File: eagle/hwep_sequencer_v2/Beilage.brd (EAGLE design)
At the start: 251.5 x 94 mm, 145 parts, among them X1 ESP32-DEVKIT-C

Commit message: i2s testing & KUB
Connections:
- new net N$1: X2.1
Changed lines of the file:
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@@
 <layer number="25" name="tNames" color="7" fill="1" visible="yes" active="yes"/>
 <layer number="26" name="bNames" color="7" fill="1" visible="yes" active="yes"/>
-<layer number="27" name="tValues" color="7" fill="1" visible="yes" active="yes"/>
-<layer number="28" name="bValues" color="7" fill="1" visible="yes" active="yes"/>
+<layer number="27" name="tValues" color="7" fill="1" visible="no" active="yes"/>
+<layer number="28" name="bValues" color="7" fill="1" visible="no" active="yes"/>
 <layer number="29" name="tStop" color="7" fill="3" visible="no" active="yes"/>
 <layer number="30" name="bStop" color="7" fill="6" visible="no" active="yes"/>
@@
 <via x="171.45" y="71.12" extent="1-16" drill="0.7" diameter="1.4"/>
 </signal>
+<signal name="N$1">
+<contactref element="X2" pad="1"/>
+</signal>
 </signals>

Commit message: removed key register visualisation
bloat feature
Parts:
- removed C24, C25: 1u, rcl_GruS:C0805
- removed C26, C27: 100n, rcl_GruS:C0805
- removed D10: STP16CP05TTR, ic_GruS:TSSOP24
- removed D11: 74AHC1G125DBV, 74xx_GruS:SOT23-5
- removed H18, H19, H20, H21, H22, H23, H24, H25, H26, H27, H28, H29, H30, H31, H32, H33: rt, led_GruS:CHIPLED_1206
- removed R27: 10k, rcl_GruS:R0805
- removed R28: 2k7, rcl_GruS:R0805
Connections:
- net CLRR renamed RKR
- removed net N$10: D10.5, H18.C
- removed net N$11: D10.6, H19.C
- removed net N$12: D10.7, H20.C
- removed net N$13: D10.8, H21.C
- removed net N$20: D10.9, H22.C
- removed net N$21: D10.10, H23.C
- removed net N$22: D10.11, H24.C
- removed net N$23: D10.12, H25.C
- removed net N$24: D10.23, R28.2
- removed net N$25: D10.13, H26.C
- removed net N$26: D10.14, H27.C
- removed net N$27: D10.15, H28.C
- removed net N$28: D10.16, H29.C
- removed net N$29: D10.17, H30.C
- removed net N$30: D10.18, H31.C
- removed net N$31: D10.19, H32.C
- removed net N$32: D10.20, H33.C
- removed net N$66: D10.4, D11.4, R27.2
- net +3V3: no longer C24.1, C25.1, C26.1, C27.1, D10.24, D11.2, D11.5, H18.A, H19.A, H20.A, H21.A, H22.A, H23.A, H24.A, H25.A, H26.A, H27.A, H28.A, H29.A, H30.A, H31.A, H32.A, H33.A
- net GND: no longer C24.2, C25.2, C26.2, C27.2, D10.1, D10.21, D11.3, R27.1, R28.1
- net MOSI: no longer D10.2
- net SCK: no longer D10.3
- net STP_LE_K: no longer D11.1
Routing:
- net N$10: track 44.8 -> 0.00 mm, vias 1 -> 0
- net N$11: track 42.0 -> 0.00 mm, vias 1 -> 0
- net SCK: track 171.0 -> 130.8 mm
- net N$12: track 39.2 -> 0.00 mm, vias 1 -> 0
- net N$13: track 36.4 -> 0.00 mm, vias 1 -> 0
- net N$29: track 34.8 -> 0.00 mm, vias 1 -> 0
- net N$30: track 34.0 -> 0.00 mm, vias 1 -> 0
- net N$28: track 33.7 -> 0.00 mm, vias 1 -> 0
- net N$20: track 33.6 -> 0.00 mm, vias 1 -> 0
- net N$27: track 33.5 -> 0.00 mm, vias 1 -> 0
- net N$26: track 33.2 -> 0.00 mm, vias 1 -> 0
- net N$31: track 33.2 -> 0.00 mm, vias 1 -> 0
- net N$32: track 31.7 -> 0.00 mm, vias 1 -> 0
- net MOSI: track 124.2 -> 92.7 mm, vias 3 -> 2
- net N$21: track 30.8 -> 0.00 mm, vias 1 -> 0
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
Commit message: upd doku
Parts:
- added FABRICATION: (no value), fabrication:FABRIACTION
- added MEASURE: (no value), fabrication:MEASURE
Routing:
- net +3V3: vias 7 -> 6

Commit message: removed unnecessary features
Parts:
- removed C2: 1u, rcl_GruS:C0805
- removed D4: 74AHC138N, 74xx_GruS:DIP16
- moved R7 55.0 mm to (232.4, 29.2)
- moved H2 54.8 mm to (234.9, 29.2)
- moved R1 35.4 mm to (226.1, 33.0), turned to 270 degrees
- moved C3 24.4 mm to (232.4, 80.0)
- moved R20 19.0 mm to (212.1, 72.4)
- moved D3 18.1 mm to (223.5, 73.7)
- moved R17 16.5 mm to (212.1, 67.3)
- moved R22 16.5 mm to (212.1, 77.5), flipped to the top, turned to 0 degrees
- moved H15 15.2 mm to (204.5, 74.9)
- moved H16 15.2 mm to (194.3, 74.9)
- moved H17 15.2 mm to (184.2, 74.9)
- moved V1 15.2 mm to (208.3, 66.0)
- moved V2 15.2 mm to (198.1, 66.0)
- moved V3 15.2 mm to (186.7, 66.0)
- moved R24 14.0 mm to (208.3, 63.5)
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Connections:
- removed net !CS!_A: D4.1, X1.29
- removed net !CS!_B: D4.2, X1.33
- removed net !CS!_C: D4.3, X1.36
- removed net 088S052_!CS!: D4.12, D5.1, R15.1
- removed net N$1: X2.1
- removed net STP_LE_K: D4.13
- removed net STP_LE_S: D13.1, D4.14
- new net ADC088S052_!CS: D5.1, R15.1, X1.33
- new net STP_!CS: D13.1, X1.36
- net +3V3: no longer C2.1, D4.16, D4.6
- net 23S08_!CS: now also X1.29; no longer D4.15
- net GND: now also X2.1; no longer C2.2, D4.4, D4.5, D4.8
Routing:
- net +3V3: track 849.4 -> 764.0 mm, vias 6 -> 5
- net 088S052_!CS!: track 82.0 -> 0.00 mm
- net ADC088S052_!CS: track 0.00 -> 72.8 mm, vias 0 -> 1
- net !CS!_A: track 71.4 -> 0.00 mm, vias 2 -> 0
- net STP_!CS: track 0.00 -> 64.7 mm, vias 0 -> 2
- net !CS!_B: track 60.9 -> 0.00 mm
- net !CS!_C: track 48.7 -> 0.00 mm, vias 1 -> 0
- net 23S08_!CS: track 82.6 -> 130.5 mm
- net STP_LE_S: track 44.6 -> 0.00 mm, vias 1 -> 0
- net 7SEG_C: track 24.9 -> 6.65 mm, vias 1 -> 0
- net 7SEG_D: track 24.1 -> 6.86 mm
- net 7SEG_G: track 22.1 -> 7.94 mm
- net 7SEG_B: track 18.3 -> 5.81 mm, vias 1 -> 0
- net 7SEG_A: track 17.8 -> 6.33 mm, vias 1 -> 0
- net 7SEG_DP: track 17.2 -> 5.81 mm, vias 1 -> 0
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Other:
- board size 251.5 x 94 mm -> 251.5 x 99.1 mm

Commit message: spi test
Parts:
- moved C3 7.73 mm to (224.8, 81.3), turned to 0 degrees
- moved H1 2.54 mm to (167.6, 83.8)
- moved R6 2.54 mm to (170.2, 83.8)
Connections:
- net ADC088S052_!CS: now also X1.23; no longer X1.33
- net INT_23S08: now also X1.36
- net STP_!CS: now also X1.33; no longer X1.36
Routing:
- net INT_23S08: track 2.14 -> 63.9 mm
- net +3V3: track 764.0 -> 822.0 mm
- net STP_!CS: track 64.7 -> 69.4 mm
- net SCK: track 140.0 -> 143.2 mm
- net 23S08_!CS: track 130.5 -> 127.7 mm
- net EVENT: track 28.1 -> 25.6 mm
- net ADC088S052_!CS: track 72.8 -> 70.9 mm
- net GND: track 31.1 -> 31.4 mm, vias 12 -> 15

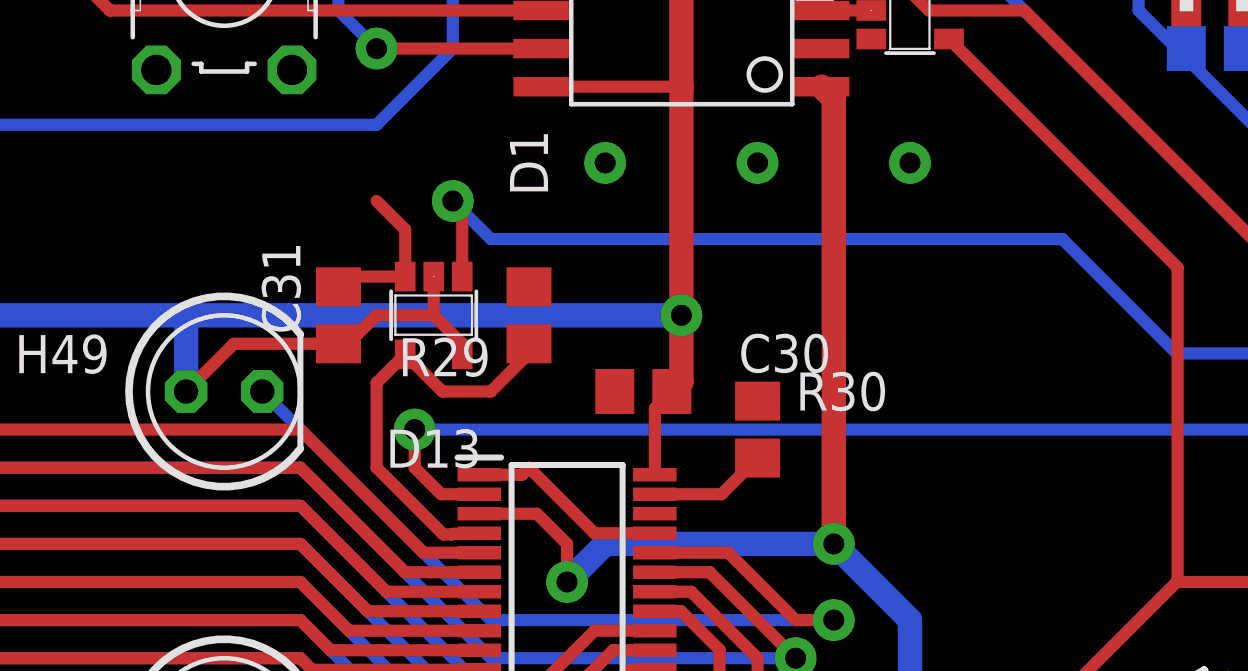
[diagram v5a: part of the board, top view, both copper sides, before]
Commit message: mcp23s08 implemented
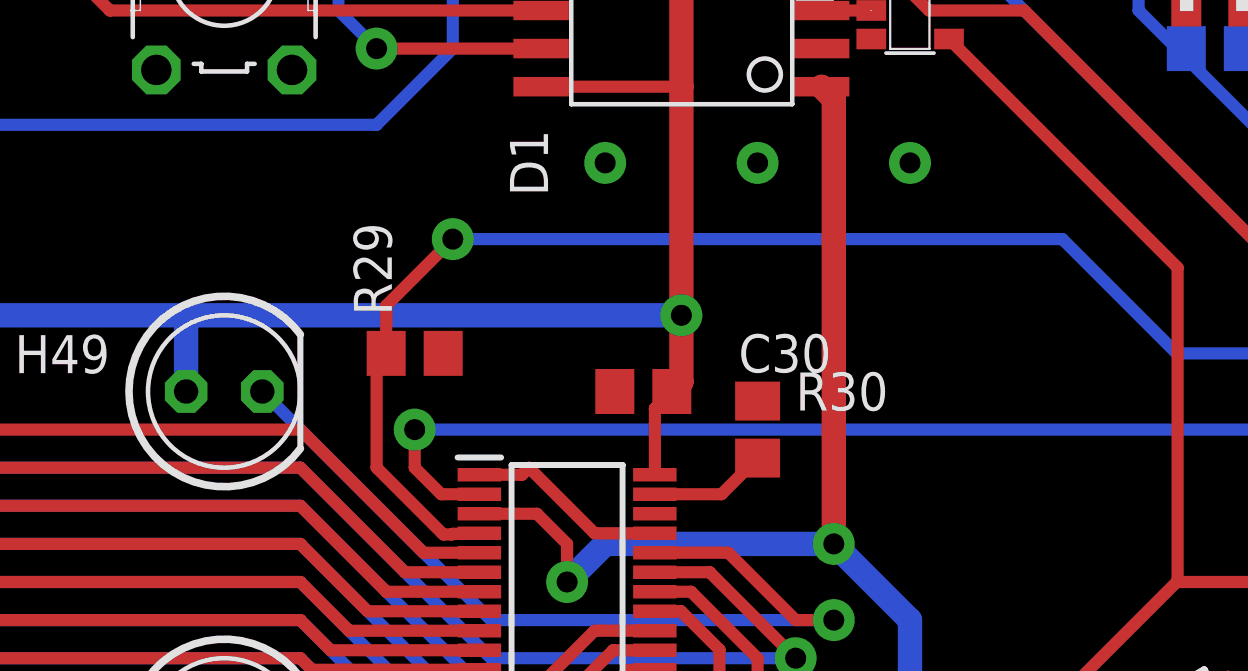
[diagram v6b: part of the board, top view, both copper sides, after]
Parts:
- removed C31: 100n, rcl_GruS:C0805
- removed D13: 74AHC1G125DBV, 74xx_GruS:SOT23-5
- moved R29 4.02 mm to (160.0, 53.3), turned to 180 degrees
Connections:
- removed net N$61: D12.4, D13.4, R29.2
- removed net STP_!CS: D13.1, X1.33
- new net STP_CS: D12.4, R29.2, X1.33
- net +3V3: no longer C31.1, D13.2, D13.5
- net GND: no longer C31.2, D13.3
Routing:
- net STP_CS: track 0.00 -> 79.3 mm, vias 0 -> 2
- net STP_!CS: track 69.4 -> 0.00 mm, vias 2 -> 0
- net N$61: track 14.0 -> 0.00 mm
- net +3V3: track 822.0 -> 809.7 mm
- net GND: track 31.4 -> 26.1 mm
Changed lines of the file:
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@@
 <attribute name="VALUE" x="168.275" y="20.32" size="1.27" layer="27" font="vector" ratio="12" rot="R180"/>
 </element>
-<element name="R29" library="rcl_GruS" library_urn="urn:adsk.eagle:library:13572313" package="R0805" package3d_urn="urn:adsk.eagle:package:18365371/1" value="10k" x="163.83" y="54.61" smashed="yes" rot="R270">
-<attribute name="NAME" x="162.56" y="53.848" size="1.27" layer="25" font="vector" ratio="12" rot="R180"/>
-<attribute name="VALUE" x="162.687" y="55.88" size="1.27" layer="27" font="vector" ratio="12" rot="R180"/>
-</element>
-<element name="C31" library="rcl_GruS" library_urn="urn:adsk.eagle:library:13572313" package="C0805" package3d_urn="urn:adsk.eagle:package:23617/2" value="100n" x="157.48" y="54.61" smashed="yes" rot="R90">
-<attribute name="CATEGORY" value="2" x="157.48" y="54.61" size="1.778" layer="27" rot="R90" display="off"/>
-<attribute name="NAME" x="156.21" y="53.975" size="1.27" layer="25" font="vector" ratio="12" rot="R90"/>
-<attribute name="VALUE" x="160.02" y="51.435" size="1.27" layer="27" font="vector" ratio="12" rot="R90"/>
+<element name="R29" library="rcl_GruS" library_urn="urn:adsk.eagle:library:13572313" package="R0805" package3d_urn="urn:adsk.eagle:package:18365371/1" value="10k" x="160.02" y="53.34" smashed="yes" rot="R180">
+<attribute name="NAME" x="159.258" y="54.61" size="1.27" layer="25" font="vector" ratio="12" rot="R90"/>
+<attribute name="VALUE" x="161.29" y="54.483" size="1.27" layer="27" font="vector" ratio="12" rot="R90"/>
 </element>
 <element name="H3" library="led_GruS" library_urn="urn:adsk.eagle:library:13581853" package="WS2812B" package3d_urn="urn:adsk.eagle:package:33577031/2" value="WS2812B" x="212.09" y="24.13" smashed="yes" rot="R90">
@@
 <attribute name="NAME" x="140.462" y="84.201" size="1.27" layer="25" ratio="10"/>
 <attribute name="VALUE" x="142.875" y="81.661" size="1.27" layer="27" ratio="10" rot="R270"/>
-</element>
-<element name="D13" library="74xx_GruS" library_urn="urn:adsk.eagle:library:13569359" package="SOT23-5" package3d_urn="urn:adsk.eagle:package:33442082/1" value="74AHC1G125DBV" x="160.655" y="54.61" smashed="yes" rot="R180">
-<attribute name="CATEGORY" value="13" x="174.625" y="46.99" size="1.778" layer="27" rot="R180" display="off"/>
-<attribute name="NAME" x="160.655" y="50.8" size="1.27" layer="25" font="vector" rot="R180" align="bottom-center"/>
-<attribute name="VALUE" x="160.655" y="52.07" size="1.27" layer="27" font="vector" rot="R180" align="bottom-center"/>
 </element>
 <element name="X4" library="con_GruS" library_urn="urn:adsk.eagle:library:13569504" package="MYLIB_SJ" package3d_urn="urn:adsk.eagle:package:33704775/1" value="" x="243.84" y="8.89" smashed="yes" rot="R180">
@@
 <via x="238.76" y="15.24" extent="1-16" drill="0.7" diameter="1.4"/>
 <contactref element="D2" pad="3"/>
-<contactref element="C31" pad="2"/>
 <contactref element="H3" pad="3"/>
 <contactref element="H6" pad="3"/>
@@
 <via x="172.72" y="77.47" extent="1-16" drill="0.7" diameter="1.4"/>
 <contactref element="S15" pad="C1"/>
-<contactref element="D13" pad="3"/>
 <contactref element="X3" pad="1"/>
 <wire x1="247.65" y1="24.13" x2="242.57" y2="24.13" width="0.8128" layer="16"/>
@@
 <wire x1="239.268" y1="24.13" x2="242.57" y2="24.13" width="0.8128" layer="16"/>
 <contactref element="R29" pad="1"/>
-<wire x1="157.48" y1="55.56" x2="157.82" y2="55.9" width="0.4064" layer="1"/>
-<wire x1="157.82" y1="55.9" x2="159.705" y2="55.9" width="0.4064" layer="1"/>
 <contactref element="X2" pad="1"/>
 <via x="176.53" y="59.69" extent="1-16" drill="0.7" diameter="1.4"/>
@@
 <via x="217.17" y="57.15" extent="1-16" drill="0.7" diameter="1.4"/>
 <via x="213.36" y="34.29" extent="1-16" drill="0.7" diameter="1.4"/>
-<wire x1="159.705" y1="55.9" x2="159.705" y2="57.465" width="0.4064" layer="1"/>
-<wire x1="159.705" y1="57.465" x2="158.75" y2="58.42" width="0.4064" layer="1"/>
 </signal>
 <signal name="RKR">
@@
 <wire x1="158.75" y1="60.96" x2="137.4394" y2="60.96" width="0.4064" layer="16"/>
 <wire x1="137.4394" y1="60.96" x2="135.6106" y2="62.7888" width="0.4064" layer="16"/>
-</signal>
-<signal name="STP_!CS">
-<contactref element="D13" pad="1"/>
-<contactref element="X1" pad="33"/>
-<wire x1="222.25" y1="44.45" x2="209.55" y2="44.45" width="0.4064" layer="1"/>
-<wire x1="209.55" y1="44.45" x2="200.66" y2="53.34" width="0.4064" layer="1"/>
-<via x="200.66" y="53.34" extent="1-16" drill="0.7" diameter="1.4"/>
-<wire x1="200.66" y1="53.34" x2="185.42" y2="53.34" width="0.4064" layer="16"/>
-<wire x1="185.42" y1="53.34" x2="181.61" y2="57.15" width="0.4064" layer="16"/>
-<wire x1="161.605" y1="55.9" x2="161.605" y2="58.105" width="0.4064" layer="1"/>
-<wire x1="161.605" y1="58.105" x2="161.29" y2="58.42" width="0.4064" layer="1"/>
-<via x="161.29" y="58.42" extent="1-16" drill="0.7" diameter="1.4"/>
-<wire x1="161.29" y1="58.42" x2="162.56" y2="57.15" width="0.4064" layer="16"/>
-<wire x1="162.56" y1="57.15" x2="181.61" y2="57.15" width="0.4064" layer="16"/>
 </signal>
 <signal name="7SEG_CH">
@@
 <contactref element="R1" pad="2"/>
 <contactref element="R15" pad="2"/>
-<contactref element="C31" pad="1"/>
 <wire x1="43.495" y1="52.07" x2="50.8" y2="52.07" width="0.8128" layer="1"/>
 <wire x1="50.8" y1="40.64" x2="43.495" y2="40.64" width="0.8128" layer="1"/>
@@
 <wire x1="106.68" y1="62.23" x2="109.22" y2="62.23" width="0.8128" layer="16"/>
 <wire x1="109.22" y1="62.23" x2="111.76" y2="62.23" width="0.8128" layer="16"/>
-<contactref element="D13" pad="2"/>
-<contactref element="D13" pad="5"/>
-<wire x1="161.605" y1="53.31" x2="161.605" y2="53.66" width="0.4064" layer="1"/>
-<wire x1="161.605" y1="53.66" x2="160.655" y2="54.61" width="0.4064" layer="1"/>
-<wire x1="160.655" y1="55.9" x2="160.655" y2="54.61" width="0.4064" layer="1"/>
 <wire x1="10.16" y1="40.64" x2="12.7" y2="38.1" width="0.8128" layer="16"/>
 <wire x1="12.7" y1="38.1" x2="30.48" y2="38.1" width="0.8128" layer="16"/>
@@
 <wire x1="121.92" y1="62.23" x2="121.92" y2="54.61" width="0.8128" layer="16"/>
 <wire x1="182.88" y1="8.89" x2="223.52" y2="8.89" width="0.8128" layer="16"/>
-<wire x1="152.4" y1="52.07" x2="153.99" y2="53.66" width="0.4064" layer="1"/>
-<wire x1="153.99" y1="53.66" x2="157.48" y2="53.66" width="0.4064" layer="1"/>
-<wire x1="157.48" y1="53.66" x2="157.8" y2="53.66" width="0.4064" layer="1"/>
-<wire x1="157.8" y1="53.66" x2="158.75" y2="54.61" width="0.4064" layer="1"/>
-<wire x1="158.75" y1="54.61" x2="160.655" y2="54.61" width="0.4064" layer="1"/>
 <wire x1="10.16" y1="40.64" x2="10.16" y2="52.07" width="0.8128" layer="16"/>
 <wire x1="242.89" y1="26.67" x2="242.89" y2="29.21" width="0.8128" layer="1"/>
@@
 <contactref element="D1" pad="3"/>
 <wire x1="175.24" y1="64.77" x2="173.585" y2="64.77" width="0.4064" layer="1"/>
-</signal>
-<signal name="N$61">
-<contactref element="D12" pad="4"/>
-<wire x1="162.175" y1="47.345" x2="162.1564" y2="47.3264" width="0.4064" layer="1"/>
-<wire x1="162.1564" y1="47.3264" x2="161.2816625" y2="47.3264" width="0.4064" layer="1"/>
-<wire x1="161.2816625" y1="47.3264" x2="161.2598625" y2="47.3046" width="0.4064" layer="1"/>
-<wire x1="160.9754" y1="47.3046" x2="158.75" y2="49.53" width="0.4064" layer="1"/>
-<wire x1="161.2598625" y1="47.3046" x2="160.9754" y2="47.3046" width="0.4064" layer="1"/>
-<contactref element="D13" pad="4"/>
-<contactref element="R29" pad="2"/>
-<wire x1="159.705" y1="53.31" x2="160.945" y2="52.07" width="0.4064" layer="1"/>
-<wire x1="162.56" y1="52.07" x2="163.83" y2="53.34" width="0.4064" layer="1"/>
-<wire x1="163.83" y1="53.34" x2="163.83" y2="53.66" width="0.4064" layer="1"/>
-<wire x1="160.945" y1="52.07" x2="162.56" y2="52.07" width="0.4064" layer="1"/>
-<wire x1="158.75" y1="49.53" x2="158.75" y2="52.355" width="0.4064" layer="1"/>
-<wire x1="158.75" y1="52.355" x2="159.705" y2="53.31" width="0.4064" layer="1"/>
 </signal>
 <signal name="N$68">
@@
 <wire x1="224.79" y1="54.61" x2="223.52" y2="55.88" width="0.4064" layer="16"/>
 </signal>
+<signal name="STP_CS">
+<contactref element="D12" pad="4"/>
+<contactref element="R29" pad="2"/>
+<wire x1="162.175" y1="47.345" x2="162.1564" y2="47.3264" width="0.4064" layer="1"/>
+<wire x1="162.1564" y1="47.3264" x2="161.2816625" y2="47.3264" width="0.4064" layer="1"/>
+<wire x1="161.2816625" y1="47.3264" x2="161.2598625" y2="47.3046" width="0.4064" layer="1"/>
+<wire x1="160.9754" y1="47.3046" x2="158.75" y2="49.53" width="0.4064" layer="1"/>
+<wire x1="161.2598625" y1="47.3046" x2="160.9754" y2="47.3046" width="0.4064" layer="1"/>
+<contactref element="X1" pad="33"/>
+<wire x1="222.25" y1="44.45" x2="209.55" y2="44.45" width="0.4064" layer="1"/>
+<wire x1="209.55" y1="44.45" x2="200.66" y2="53.34" width="0.4064" layer="1"/>
+<via x="200.66" y="53.34" extent="1-16" drill="0.7" diameter="1.4"/>
+<wire x1="200.66" y1="53.34" x2="185.42" y2="53.34" width="0.4064" layer="16"/>
+<wire x1="185.42" y1="53.34" x2="181.61" y2="57.15" width="0.4064" layer="16"/>
+<via x="161.29" y="57.15" extent="1-16" drill="0.7" diameter="1.4"/>
+<wire x1="161.29" y1="57.15" x2="181.61" y2="57.15" width="0.4064" layer="16"/>
+<wire x1="158.75" y1="49.53" x2="158.75" y2="53.02" width="0.4064" layer="1"/>
+<wire x1="158.75" y1="53.02" x2="159.07" y2="53.34" width="0.4064" layer="1"/>
+<wire x1="159.07" y1="53.34" x2="159.07" y2="54.93" width="0.4064" layer="1"/>
+<wire x1="159.07" y1="54.93" x2="161.29" y2="57.15" width="0.4064" layer="1"/>
+</signal>
 </signals>

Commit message: reroute brd complete
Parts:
- X1: value ESP32-DEVKIT-C -> ESP32CLIP2122; device modul_GruS:ESP32-DEVKIT-C -> modul_GruS:ESP32-DEVKIT-C-CLIP
- moved R1 80.1 mm to (153.7, 67.3), flipped to the bottom, turned to 90 degrees
- moved H2 79.6 mm to (168.9, 73.7), turned to 90 degrees
- moved R7 79.0 mm to (168.9, 76.2), turned to 180 degrees
- moved C4 78.6 mm to (220.3, 67.3), turned to 0 degrees
- moved X1 73.3 mm to (176.5, 74.9), turned to 270 degrees
- moved X4 65.9 mm to (222.2, 71.1), flipped to the bottom, turned to 270 degrees
- moved R12 63.8 mm to (207.0, 78.7), turned to 90 degrees
- moved R13 63.3 mm to (204.5, 78.7), turned to 90 degrees
- moved R14 63.0 mm to (201.9, 78.7), turned to 90 degrees
- moved C3 62.5 mm to (168.9, 53.3), flipped to the bottom, turned to 270 degrees
- moved D3 60.8 mm to (163.8, 62.2), flipped to the bottom
- moved X3 52.4 mm to (218.4, 71.1)
- moved R15 51.6 mm to (207.0, 53.3), turned to 180 degrees
- moved R23 41.9 mm to (172.2, 67.3), flipped to the bottom
- moved R19 41.2 mm to (172.2, 62.2), flipped to the bottom
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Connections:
- removed net N$71: H11.4, H8.2
- removed net N$8: D9.4, H3.4
- new net DI: D9.4, H11.4
- new net DO: H14.2, H3.4
- net AGND: now also X1.22
- net VREF: now also X1.21
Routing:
- net +3V3: track 809.7 -> 678.4 mm, vias 5 -> 6
- net 23S08_!CS: track 127.7 -> 55.1 mm
- net 7SEG_CH: track 77.7 -> 6.23 mm, vias 1 -> 0
- net 7SEG_CZ: track 67.4 -> 5.70 mm, vias 2 -> 0
- net 7SEG_CE: track 62.2 -> 5.96 mm, vias 2 -> 0
- net SCK: track 143.2 -> 89.6 mm, vias 3 -> 2
- net STP_CS: track 79.3 -> 31.1 mm, vias 2 -> 1
- net MOSI: track 85.8 -> 38.3 mm, vias 1 -> 2
- net INT_23S08: track 63.9 -> 19.3 mm
- net N$7: track 26.6 -> 68.8 mm, vias 0 -> 1
- net N$8: track 32.5 -> 0.00 mm
- net MISO: track 94.4 -> 65.7 mm
- net PL_DIN: track 3.79 -> 30.6 mm
- net AGND: track 276.2 -> 302.2 mm, vias 1 -> 2
- net ADC088S052_!CS: track 70.9 -> 93.1 mm
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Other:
- board size 251.5 x 99.1 mm -> 227.3 x 82.5 mm

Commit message: optimized brd and 3d model
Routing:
- net N$7: track 68.8 -> 37.2 mm
- net N$55: track 30.6 -> 23.9 mm
- net N$65: track 20.6 -> 22.7 mm
- net N$33: track 36.3 -> 34.5 mm
- net EC11_B: track 79.1 -> 78.1 mm
- net PL_DIN: track 30.6 -> 29.5 mm
- net N$56: track 34.9 -> 35.8 mm
- net N$35: track 31.4 -> 30.7 mm
